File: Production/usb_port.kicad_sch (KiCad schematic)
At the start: 106 parts, among them J401 TYPE-C 16PCB1.6 IP68, Q401 PGQ04N070, Q402 PGQ04N070, Q403 AO3401A, Q404 AO3401A, Q405 AO3400A, Q406 AO3400A, Q407 PGQ04N070, Q408 PGQ04N070, U401 TPS25751DREFR, U402 M24512-DFMC6TG, U403 BQ25756RRVR, U404 TPS62933DRLR, U405 TPD4S201TRGRRQ1

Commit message: Production schematic P0: drawing tidy
tools/tidy_production.py (runs after make_production.py): pogo pads in their
own row, TC2030 under its SWD heading, link-merge leftovers removed, empty
headings deleted, sheet notes, root index and revision log rewritten for
production, sheets renamed 3V3 Rail and MCU. Netlist unchanged (check_netlist
passes); ERC: no errors.

Co-Authored-By: Claude Opus 5.5 <noreply@anthropic.com>
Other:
- note added: "FACTORY TEST PAD"
- note added: "GATE RESISTORS + TURN-OFF DIODES"
- note added: "PP5V SUPPLY TPS62933 (1.2 MHz, 5.16 V) - 5 V source + VCONN"
- note removed: "GATE / BOOTSTRAP TUNING (BQ25756EVM fig. 3-1: R8, R20, R3, R17, R13, R23, snubbers)"
- note removed: "PP5V SUPPLY TPS62933 (1.2 MHz, 5.08 V) - 5 V source + VCONN"
- note removed: "TEST POINTS / POWER FLAGS"
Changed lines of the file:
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@@
 		(company "Monolith 100 W battery bank - production")
 		(comment 1 "TPS25751D + BQ25756 + TPS62933; port 1 = 4xx, port 2 = 5xx")
-		(comment 2 "Spec + open items: DevBoard/README.md")
+		(comment 2 "Spec + open items: Production/README.md")
 		(comment 3 "P0: dev board rev A8 stripped by Production/tools/make_production.py; not reviewed")
 	)
-	(text "PP5V SUPPLY  TPS62933 (1.2 MHz, 5.08 V)  - 5 V source + VCONN"
+	(text "PP5V SUPPLY  TPS62933 (1.2 MHz, 5.16 V)  - 5 V source + VCONN"
 		(exclude_from_sim no)
 		(at 40.64 186.69 0)
@@
 		)
 	)
-	(text "GATE / BOOTSTRAP TUNING  (BQ25756EVM fig. 3-1: R8, R20, R3, R17, R13, R23, snubbers)"
+	(text "GATE RESISTORS + TURN-OFF DIODES"
 		(exclude_from_sim no)
 		(at 299.72 264.16 0)
@@
 		)
 	)
-	(text "TEST POINTS / POWER FLAGS"
+	(text "FACTORY TEST PAD"
 		(exclude_from_sim no)
 		(at 40.64 276.86 0)
@@
 	(text "Charger battery side joins PACK_P here (net tie R430 removed).\nRoute SRN (R429) and the FB divider top (R418) from R427's PACK_P pad,\nnot from the pour: DRC can't catch a tap on the bus."
 		(exclude_from_sim no)
-		(at 448.31 50.8 0)
+		(at 459.74 35.56 0)
 		(effects
 			(font
@@
 		)
 	)
-	(text "NOTES  (this sheet is used twice: USB Port 1 = 4xx, USB Port 2 = 5xx)\n1. Address straps are on the root sheet: port 1 ADCIN1 = LDO_3V3, ADCIN2 = GND (0x20);\n   port 2 ADCIN1 = ADCIN2 = GND (0x21). Both are SafeMode (TPS25751 table 8-6).\n2. Unused TPS25751 GPIOs (0, 1, 2, 11) tied to GND per datasheet (KiCad ERC flags this; expected).\n   Never configure them as outputs.\n3. CC and SBU are protected by U405 (TPD4S201, below); C401/C402 (220 pF) on the controller side. D+/D- are shorted by R440 (passive BC1.2 DCP); the TPS25751\n   no longer does BC1.2. Liquid detection (TI fig. 9-8): GPIO4/5 read SBU1/2 through U405 (TPD4S201: CC and SBU OVP + ESD);\n   GPIO6 = liquid_pmos_control (LIQ_PU), GPIO7 = liquid_nmos_control (LIQ_PD) in the TPS25751 configuration.\n   U405 FLT -> GPIO3 = Fault_Input_Event (SBU_FLT, R441): an SBU short to VBUS forces error recovery.\n   R442/R443 hold the liquid-detect FETs off while GPIO6/7 are Hi-Z. TP415-TP421: CC, SBU and liquid-detect probes.\n   D401 = TVS2200 flat clamp on VBUS (28 V at 40 A 8/20 us; TI's pick for the TPS25751).\n4. Kelvin-route ACP/ACN from R424 and SRP/SRN from R427; filter parts at the IC.\n5. Two MLCCs of each bulk bank plus C430/C438 at the FETs; the bulk caps (C421 polymer, C432 hybrid polymer) and remaining MLCCs\n   one row back. Polymer carries the bulk (no DC-bias loss), MLCCs carry the switching-frequency ripple.\n6. I2Cc pull-ups go to this TPS25751's own LDO_3V3 (TI guidance).\n7. The charger battery side is PACK_P directly (net tie R430 removed 2026-10-16); take SRN/FB from R427's pad.\n8. VAC is taken before R424 per TI typical application; DRV_SUP fed from REGN via R420.\n9. PPHV bulk (BQ25756 input bank) exceeds the 100 uF USB PD cSnkBulkPd: the TPS25751D sink switch soft-start limits\n   inrush (C x SS: about 125 uF effective x 0.47 V/ms max = 0.06 A at SS setting 0).\n   Set PPHV soft-start to setting 0 or 1 in the TPS25751 configuration.\n10. Diamonds are PWR_FLAGs (ERC only, no part): each sits where its rail is sourced through a passive part.\n11. CHG_INH (rev A5): R417 pulls CE up to 3V3, so charging needs the MCU (DIO24) to drive CHG_INH low through R435.\n    Reset, WDT reset, the ROM bootloader or an unprogrammed MCU stop charging; CC2340 Standby keeps the pin state.\n    A dead pack (3V3 down) still charges. Keep DIS_CE_PIN = 0.\n12. Tuning block (review 3): R444-R449 0R in the gate and BTST lines, R450/C454 and R451/C455 DNP snubbers (R 1206 0.66 W).\n    Place the 0R right at the FET gates / BTST pins; they are where a few ohms go if the edges ring."
+	(text "NOTES  (this sheet is used twice: USB Port 1 = 4xx, USB Port 2 = 5xx)\n1. Address straps are on the root sheet: port 1 ADCIN1 = LDO_3V3, ADCIN2 = GND (0x20);\n   port 2 ADCIN1 = ADCIN2 = GND (0x21). Both are SafeMode (TPS25751 table 8-6).\n2. Unused TPS25751 GPIOs (0, 1, 2, 11) tied to GND per datasheet (KiCad ERC flags this; expected).\n   Never configure them as outputs.\n3. CC and SBU are protected by U405 (TPD4S201, below); C401/C402 (220 pF) on the controller side.\n   D+ and D- are tied together at the connector (net DPDN_DCP: passive BC1.2 DCP); the TPS25751 does no BC1.2.\n   Liquid detection (TI fig. 9-8): GPIO4/5 read SBU1/2 through U405 (TPD4S201: CC and SBU OVP + ESD);\n   GPIO6 = liquid_pmos_control (LIQ_PU), GPIO7 = liquid_nmos_control (LIQ_PD) in the TPS25751 configuration.\n   U405 FLT -> GPIO3 = Fault_Input_Event (SBU_FLT, R441): an SBU short to VBUS forces error recovery.\n   R442/R443 hold the liquid-detect FETs off while GPIO6/7 are Hi-Z.\n   D401 = TVS2200 flat clamp on VBUS (28 V at 40 A 8/20 us; TI's pick for the TPS25751).\n4. Kelvin-route ACP/ACN from R424 and SRP/SRN from R427; filter parts at the IC.\n5. Two MLCCs of each bulk bank plus C430/C438 at the FETs; the bulk caps (C421 polymer, C432 hybrid polymer) and remaining MLCCs\n   one row back. Polymer carries the bulk (no DC-bias loss), MLCCs carry the switching-frequency ripple.\n6. I2Cc pull-ups go to this TPS25751's own LDO_3V3 (TI guidance).\n7. The charger battery side is PACK_P directly; take SRN/FB from R427's pad, not from the pour.\n8. VAC is taken before R424 per TI typical application; DRV_SUP fed from REGN via R420.\n9. PPHV bulk (BQ25756 input bank) exceeds the 100 uF USB PD cSnkBulkPd: the TPS25751D sink switch soft-start limits\n   inrush (C x SS: about 125 uF effective x 0.47 V/ms max = 0.06 A at SS setting 0).\n   Set PPHV soft-start to setting 0 or 1 in the TPS25751 configuration.\n10. Diamonds are PWR_FLAGs (ERC only, no part): each sits where its rail is sourced through a passive part.\n11. CHG_INH: R417 pulls CE up to 3V3, so charging needs the MCU (DIO24) to drive CHG_INH low through R435.\n    Reset, WDT reset, the ROM bootloader or an unprogrammed MCU stop charging; CC2340 Standby keeps the pin state.\n    A dead pack (3V3 down) still charges. Keep DIS_CE_PIN = 0.\n12. Gate drive: R444-R447 10R at the FET gates with D406-D409 for fast turn-off. BTST is wired straight to its cap\n    and there are no snubbers (removed in P0 before any bring-up data: add them back if the dev board shows ringing).\n13. TP401 VBUS is a factory test pad."
 		(exclude_from_sim no)
 		(at 299.72 368.3 0)
@@
 	(wire
 		(pts
-			(xy 76.2 195.58) (xy 86.36 195.58)
-		)
-		(stroke
-			(width 0)
-			(type default)
-		)
-	)
-	(wire
-		(pts
 			(xy 220.98 67.31) (xy 209.55 67.31)
 		)
@@
 	(wire
 		(pts
-			(xy 130.81 71.12) (xy 137.16 71.12)
-		)
-		(stroke
-			(width 0)
-			(type default)
-		)
-	)
-	(wire
-		(pts
 			(xy 149.86 99.06) (xy 144.78 99.06)
 		)
@@
 	(wire
 		(pts
-			(xy 86.36 195.58) (xy 93.98 195.58)
-		)
-		(stroke
-			(width 0)
-			(type default)
-		)
-	)
-	(wire
-		(pts
 			(xy 438.15 231.14) (xy 441.96 231.14)
 		)
@@
 		)
 	)
-	(label "BTST2"
-		(at 341.63 279.4 180)
-		(effects
-			(font
-				(size 1.27 1.27)
-			)
-			(justify right bottom)
-		)
-	)
 	(label "I2CC_SCL"
 		(at 185.42 109.22 0)
@@
 		)
 	)
-	(label "BTST1"
-		(at 341.63 271.78 180)
-		(effects
-			(font
-				(size 1.27 1.27)
-			)
-			(justify right bottom)
-		)
-	)
 	(label "STAT2"
 		(at 365.76 205.74 180)
@@
 	(wire
 		(pts
-			(xy 123.19 71.12) (xy 130.81 71.12)
-		)
-		(stroke
-			(width 0)
-			(type default)
-		)
-	)
-	(wire
-		(pts
 			(xy 40.64 195.58) (xy 50.8 195.58)
 		)
@@
 		)
 	)
-	(wire
-		(pts
-			(xy 87.63 106.68) (xy 95.25 106.68)
-		)
-		(stroke
-			(width 0)
-			(type default)
-		)
-	)
-	(wire
-		(pts
-			(xy 341.63 271.78) (xy 349.25 271.78)
-		)
-		(stroke
-			(width 0)
-			(type default)
-		)
-	)
-	(wire
-		(pts
-			(xy 341.63 279.4) (xy 349.25 279.4)
-		)
-		(stroke
-			(width 0)
-			(type default)
-		)
-	)
 	(label "BTST2"
 		(at 401.32 190.5 180)
@@
 		(in_pos_files yes)
 		(dnp no)
-		(property "Reference" "#PWR9027"
+		(property "Reference" "#PWR9029"
 			(at 154.94 78.74 0)
 			(hide yes)
@@
 			(project "Monolith"
 				(path "/f83241ae-2bb3-4ed7-b986-c0a03971de0a/5279a7a1-113d-4a80-b1cf-737ba19b6809"
-					(reference "#PWR9028")
+					(reference "#PWR9030")
 					(unit 1)
 				)
 				(path "/f83241ae-2bb3-4ed7-b986-c0a03971de0a/ac72c9a4-7723-4f18-89ba-289142807a08"
-					(reference "#PWR9029")
+					(reference "#PWR9031")
 					(unit 1)
 				)
@@
 		(in_pos_files yes)
 		(dnp no)
-		(property "Reference" "#PWR9030"
+		(property "Reference" "#PWR9032"
 			(at 50.8 195.58 0)
 			(hide yes)
@@
 			(project "Monolith"
 				(path "/f83241ae-2bb3-4ed7-b986-c0a03971de0a/5279a7a1-113d-4a80-b1cf-737ba19b6809"
-					(reference "#PWR9031")
+					(reference "#PWR9033")
 					(unit 1)
 				)
 				(path "/f83241ae-2bb3-4ed7-b986-c0a03971de0a/ac72c9a4-7723-4f18-89ba-289142807a08"
-					(reference "#PWR9032")
+					(reference "#PWR9034")
 					(unit 1)
 				)
@@
 		)
 	)
-	(label "BTST2"
-		(at 349.25 279.4 0)
-		(effects
-			(font
-				(size 1.27 1.27)
-			)
-			(justify left bottom)
-		)
-	)
 	(label "BTST1"
 		(at 401.32 177.8 180)
@@
 	)
 	(label "DPDN_DCP"
-		(at 95.25 106.68 0)
-		(effects
-			(font
-				(size 1.27 1.27)
-			)
-			(justify left bottom)
-		)
-	)
-	(label "DPDN_DCP"
 		(at 60.96 99.06 0)
 		(effects
@@
 		)
 	)
-	(label "DPDN_DCP"
-		(at 87.63 106.68 180)
-		(effects
-			(font
-				(size 1.27 1.27)
-			)
-			(justify right bottom)
+	(wire
+		(pts
+			(xy 76.2 195.58) (xy 93.98 195.58)
+		)
+		(stroke
+			(width 0)
+			(type default)
 		)
 	)
-	(label "BTST1"
-		(at 349.25 271.78 0)
-		(effects
-			(font
-				(size 1.27 1.27)
-			)
-			(justify left bottom)
+	(wire
+		(pts
+			(xy 137.16 71.12) (xy 123.19 71.12)
+		)
+		(stroke
+			(width 0)
+			(type default)
 		)
 	)

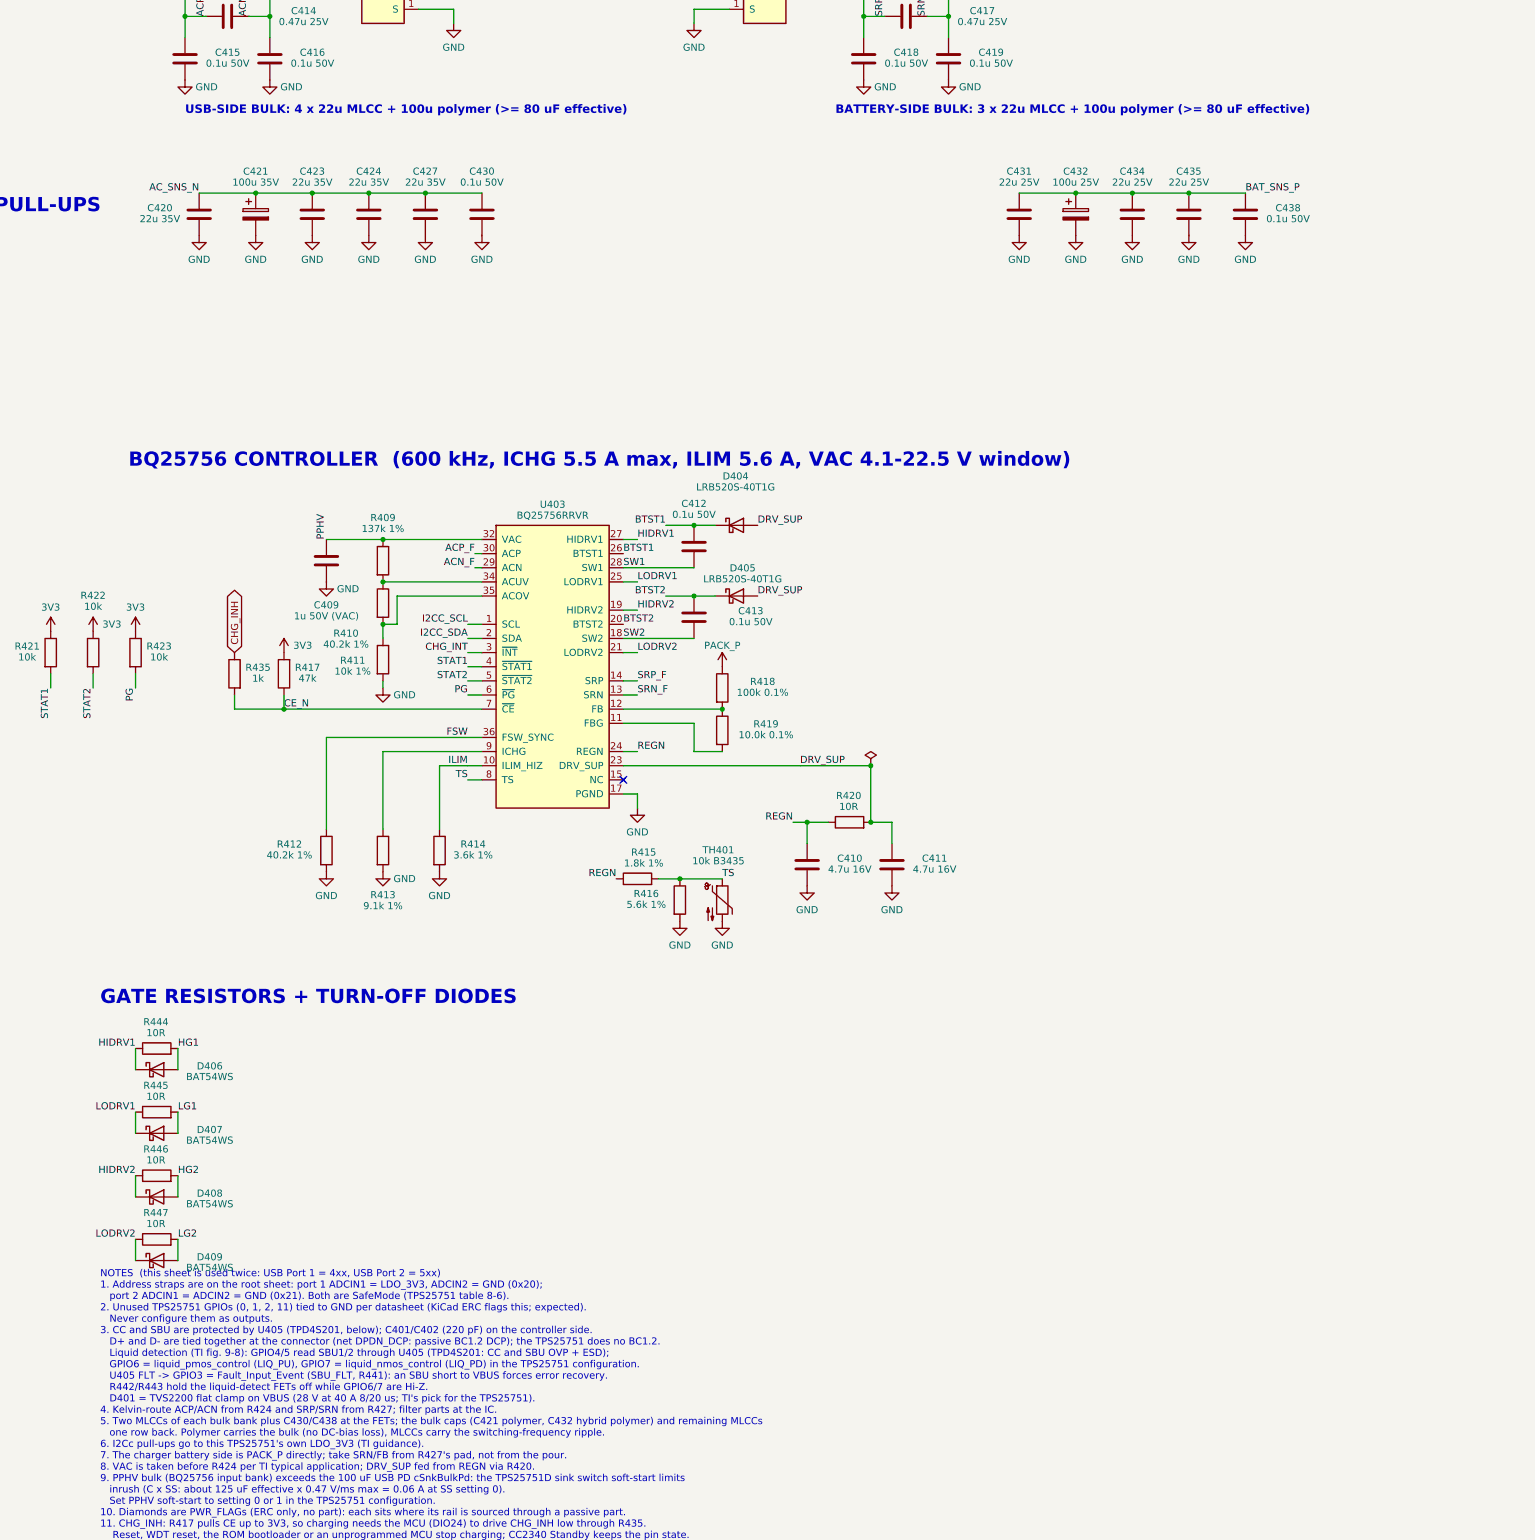
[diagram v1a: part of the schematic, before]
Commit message: Production schematic P0: drop C435/C535 (cap sims B2)
Battery-side charger bank goes to 2 x 22u 1206 + 100u hybrid: 87 uF effective
(>= 80 uF), hybrid at 63 % of its ripple rating. C427 and C443 stay on hold
(bring-up and the cSrcBulkShared question). Netlist check passes; ERC clean.

Co-Authored-By: Claude Opus 5.5 <noreply@anthropic.com>
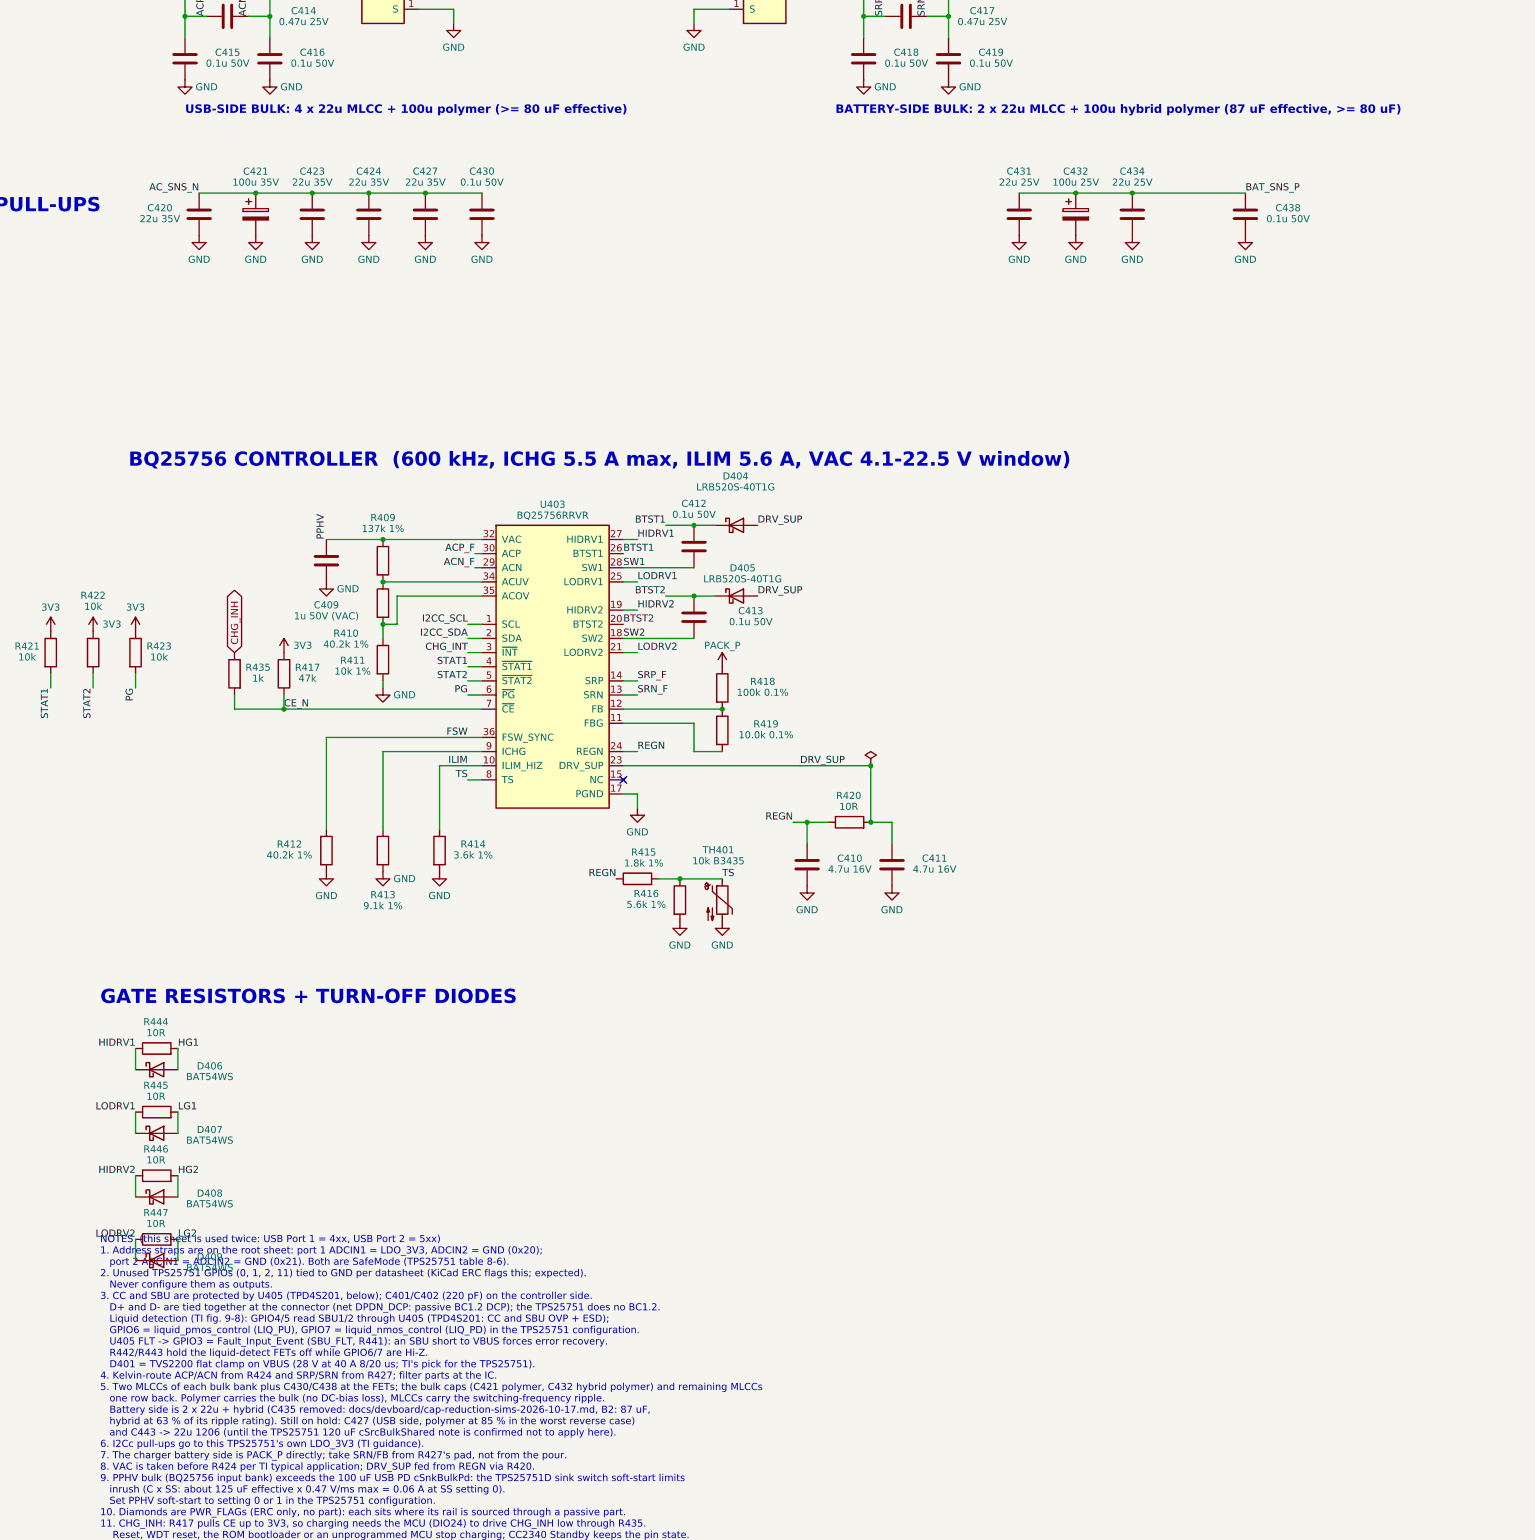
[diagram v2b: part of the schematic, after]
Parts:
- removed C435: 22u 25V, Capacitor_SMD:C_1206_3216Metric, symbol Device:C
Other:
- note added: "BATTERY-SIDE BULK: 2 x 22u MLCC + 100u hybrid polymer (87 uF effective, >= 80 uF)"
- note removed: "BATTERY-SIDE BULK: 3 x 22u MLCC + 100u polymer (>= 80 uF effective)"
